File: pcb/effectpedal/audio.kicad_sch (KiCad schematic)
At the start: 5 parts

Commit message: Made progress on the PCB
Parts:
- removed J?: SJ2-3574A-SMT-TR, SJ23574ASMTTR, symbol SJ2-3574A-SMT-TR:SJ2-3574A-SMT-TR
- added C1, C2, C3, C4, C5, C6: 47u, Capacitor_SMD:C_1210_3225Metric, symbol Device:C_Small
- added C10, C11, C7, C8, C9: 0.1u, Capacitor_SMD:C_0805_2012Metric, symbol Device:C_Small
- added C12, C13: 33p, Capacitor_SMD:C_0805_2012Metric, symbol Device:C_Small
- added D1, D2, D3, D4: D_Schottky, Diode_SMD:D_0805_2012Metric, symbol Device:D_Schottky
- added J1, J2, J3: SJ-43515RS-SMT-TR, footprints:SJ43515RSSMTTR, symbol SJ-43515RS-SMT-TR:SJ-43515RS-SMT-TR
- added J10: Conn_01x06_Male, Connector_PinHeader_2.54mm:PinHeader_1x06_P2.54mm_Vertical, symbol Connector:Conn_01x06_Male
- added J11, J7, J8: Conn_01x04_Female, Connector_PinSocket_2.54mm:PinSocket_1x04_P2.54mm_Vertical, symbol Connector:Conn_01x04_Female
- added J4, J5, J6, J9: Conn_01x06_Female, Connector_PinSocket_2.54mm:PinSocket_1x06_P2.54mm_Vertical, symbol Connector:Conn_01x06_Female
- added JP1, JP10, JP11, JP12, JP13, JP14, JP16, JP17, JP18, JP19, JP20, JP22, JP23, JP24, JP25, JP26, JP29, JP30, JP31, JP4, JP49, JP5, JP50, JP6, JP7, JP8: SolderJumper_2_Open, Jumper:SolderJumper-2_P1.3mm_Open_Pad1.0x1.5mm, symbol Jumper:SolderJumper_2_Open
- added JP15, JP21, JP27, JP28, JP3, JP32, JP9: SolderJumper_2_Bridged, Jumper:SolderJumper-2_P1.3mm_Bridged2Bar_Pad1.0x1.5mm, symbol Jumper:SolderJumper_2_Bridged
- added R1, R2: 10k, Resistor_SMD:R_0805_2012Metric, symbol Device:R
- added R10, R11, R8, R9: 4k, Resistor_SMD:R_0805_2012Metric, symbol Device:R
- added R3, R5, R6, R7: 27, Resistor_SMD:R_0805_2012Metric, symbol Device:R_Small
- added R4: 10, Resistor_SMD:R_0805_2012Metric, symbol Device:R_Small
- added TP10, TP6, TP7, TP9: TestPoint, TestPoint:TestPoint_Pad_D1.0mm, symbol Connector:TestPoint
- IC1: renamed from IC?; footprint SOIC127P600X175-8N -> footprints:SOIC127P600X175-8N
- U1: renamed from U?; footprint QFN50P500X500X100-33N -> footprints:QFN50P500X500X100-33N
- U2, U3: renamed from U?; value SC0915 -> Pi Pico; footprint MODULE_SC0915 -> footprints:MODULE_SC0915
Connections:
- net MCU_DBG_TX: now reaches U2.1 (GP0)
- net MCU_DBG_TX: now also U3.7 (GP5), J10.3 (Pin_3)
- net MN_UI-INT: now reaches U2.10 (GP7)
- net MN_UI-INT: now also J9.6 (Pin_6)
- net MN_EX3: now reaches U2.11 (GP8)
- net MN_EX3: now also U3.11 (GP8), J5.2 (Pin_2), JP50.2 (B)
- net at U2.12 (GP9): now also IC1.1 (CE#)
- net GND3: now reaches U2.13 (GND), U2.18 (GND), U2.23 (GND), U2.28 (GND), U2.3 (GND), U2.38 (GND), U2.8 (GND), U2.D2 (GND)
- net GND3: now also IC1.4 (VSS), U1.12 (SPI_SELECT), U1.28 (DVSS), U1.33 (EP), U1.7 (IOVSS), U3.13 (GND), U3.18 (GND), U3.23 (GND), U3.28 (GND), U3.3 (GND), U3.38 (GND), U3.8 (GND), U3.D2 (GND), C10.1, C11.1, C9.1, J10.1 (Pin_1), J11.1 (Pin_1), J11.2 (Pin_2), J5.1 (Pin_1), J6.1 (Pin_1), J6.2 (Pin_2), J6.3 (Pin_3), J7.1 (Pin_1), J7.2 (Pin_2), J7.3 (Pin_3), J8.1 (Pin_1), J9.1 (Pin_1), JP30.1 (A), JP31.1 (A)
- net at U2.14 (GP10): now also IC1.6 (CLK)
- net at U2.15 (GP11): now also IC1.5 (SI/SIO0)
- net MN_EX4: now reaches U2.16 (GP12)
- net MN_EX4: now also U3.12 (GP9), J5.5 (Pin_5), JP49.2 (B)
- net at U2.17 (GP13): now also IC1.7 (SIO3)
- net MN_EX1: now reaches U2.19 (GP14)
- net MN_EX1: now also U3.9 (GP6), J5.3 (Pin_3)
- net MCU_DBG_RX: now reaches U2.2 (GP1)
- net MCU_DBG_RX: now also U3.6 (GP4), J10.4 (Pin_4)
- net MN_EX2: now reaches U2.20 (GP15)
- net MN_EX2: now also U3.10 (GP7), J5.4 (Pin_4)
- net at U2.21 (GP16): now also JP3.1 (A), JP4.1 (A), JP5.1 (A), JP6.1 (A), JP7.1 (A)
- net at U2.22 (GP17): now also JP10.1 (A), JP11.1 (A), JP12.1 (A), JP8.1 (A), JP9.1 (A)
- net at U2.24 (GP18): now also JP13.1 (A), JP14.1 (A), JP15.1 (A), JP16.1 (A), JP17.1 (A)
- net at U2.25 (GP19): now also JP18.1 (A), JP19.1 (A), JP20.1 (A), JP21.1 (A), JP22.1 (A)
- net at U2.26 (GP20): now also JP23.1 (A), JP24.1 (A), JP25.1 (A), JP26.1 (A), JP27.1 (A)
- net AUDIO_INT1: now reaches U2.27 (GP21)
- net AUDIO_INT1: now also U1.11 (MISO/MFP4)
- net AUDIO_INT2: now reaches U2.29 (GP22)
- net AUDIO_INT2: now also U1.32 (GPIO/MFP5_(32))
- net ADC0: now reaches U2.31 (GP26)
- net ADC0: now also J4.1 (Pin_1)
- net ADC1: now reaches U2.32 (GP27)
- net ADC1: now also J4.3 (Pin_3)
- net MN_AGND: now reaches U2.33 (AGND)
- net MN_AGND: now also J4.2 (Pin_2), J4.4 (Pin_4), JP30.2 (B)
- net ADC2: now reaches U2.34 (GP28)
- net ADC2: now also J4.5 (Pin_5)
- net MN_3V3: now reaches U2.36 (3V3_OUT)
- net MN_3V3: now also IC1.8 (VDD), U1.26 (LDOIN), U1.30 (LDO_SELECT), U1.6 (IOVDD), C11.2, C9.2, J10.2 (Pin_2), J11.3 (Pin_3), J11.4 (Pin_4), J4.6 (Pin_6), J5.6 (Pin_6), J6.4 (Pin_4), J6.5 (Pin_5), J6.6 (Pin_6), J8.2 (Pin_2), J9.2 (Pin_2), JP29.1 (A), JP32.2 (B), R10.1, R11.1, R8.1, R9.1
- net MN_UI-SDA: now reaches U2.4 (GP2)
- net MN_UI-SDA: now also J8.3 (Pin_3), J9.3 (Pin_3), R8.2
- net MN_UI-SCL: now reaches U2.5 (GP3)
- net MN_UI-SCL: now also J8.4 (Pin_4), J9.4 (Pin_4), R9.2
- net AUDIO-SDA: now reaches U2.6 (GP4)
- net AUDIO-SDA: now also U1.10 (SDA/MOSI), R10.2
- net AUDIO-SCL: now reaches U2.7 (GP5)
- net AUDIO-SCL: now also U1.9 (SCL/SSZ), R11.2
- net MN_RST: now reaches U2.9 (GP6)
- net MN_RST: now also J7.4 (Pin_4), J9.5 (Pin_5), JP28.2 (B)
- net DBG_SWCLK: now reaches U2.D1 (SWCLK)
- net DBG_SWCLK: now also U3.4 (GP2), J10.6 (Pin_6)
- net DBG_SWDIO: now reaches U2.D3 (SWDIO)
- net DBG_SWDIO: now also U3.5 (GP3), J10.5 (Pin_5)
- net at IC1.2 (SO/SIO1): now also JP50.1 (A)
- net at IC1.3 (SIO2): now also JP49.1 (A)
- net AUDIO_MCLK: now reaches U1.1 (MCLK_(1))
- net AUDIO_MCLK: now also R4.2
- net AUDIO_IN_L: now reaches U1.13 (IN1_L)
- net AUDIO_IN_L: now also C1.1, C12.2, D1.2 (A), D2.1 (K)
- net AUDIO_IN_R: now reaches U1.14 (IN1_R)
- net AUDIO_IN_R: now also C13.2, C6.1, D3.2 (A), D4.1 (K)
- net AUDIO_AGND: now reaches U1.15 (IN2_L)
- net AUDIO_AGND: now also U1.16 (IN2_R), U1.17 (AVSS), U1.20 (IN3_L), U1.21 (IN3_R), C12.1, C13.1, C7.2, C8.1, D2.2 (A), D4.2 (A), J1.1 (SLEEVE), J1.4 (RING_2_), J2.1 (SLEEVE), J3.1 (SLEEVE), J3.4 (RING_2_), JP1.1 (A), JP31.2 (B), R1.2, R2.2
- net at U1.18 (REF): now also C7.1
- net at U1.2 (BCLK): now also R5.2
- net AUDIO_LINE_L: now reaches U1.22 (LOL)
- net AUDIO_LINE_L: now also C4.1, TP10.1
- net AUDIO_LINE_R: now reaches U1.23 (LOR)
- net AUDIO_LINE_R: now also C5.1, TP7.1
- net AUDIO_AVDD: now reaches U1.24 (AVDD)
- net AUDIO_AVDD: now also C8.2, D1.1 (K), D3.1 (K)
- net HEADPHONE_L: now reaches U1.25 (HPL)
- net HEADPHONE_L: now also C2.1, TP9.1
- net HEADPHONE_R: now reaches U1.27 (HPR)
- net HEADPHONE_R: now also C3.1, TP6.1
- net at U1.29 (DVDD): now also C10.2
- net at U1.3 (WCLK): now also R7.2
- net at U1.31 (~RESET): now also JP28.1 (A), JP29.2 (B)
- net AUDIO_DIN: now reaches U1.4 (DIN/MFP1)
- net AUDIO_DIN: now also R3.1
- net at U1.5 (DOUT/MFP2): now also R6.1
- net HEADSET_DETECT: now reaches U1.8 (SCLK/MFP3)
- net HEADSET_DETECT: now also J2.4 (RING_2_), JP1.2 (B)
- net at U3.36 (3V3_OUT): now also JP32.1 (A)
- new net: C1.2, J1.2 (TIP), R1.1
- new net: C5.2, J3.3 (RING_1)
- new net: C3.2, J2.3 (RING_1)
- new net: JP11.2 (B), JP16.2 (B), JP21.2 (B), JP26.2 (B), JP6.2 (B), R3.2
- new net: C4.2, J3.2 (TIP)
- new net: C6.2, J1.3 (RING_1), R2.1
- new net: JP13.2 (B), JP18.2 (B), JP23.2 (B), JP3.2 (B), JP8.2 (B), R4.1
- new net: C2.2, J2.2 (TIP)
- new net AUDIO_BCLK: JP14.2 (B), JP19.2 (B), JP24.2 (B), JP4.2 (B), JP9.2 (B), R5.1
- new net AUDIO_DOUT: JP12.2 (B), JP17.2 (B), JP22.2 (B), JP27.2 (B), JP7.2 (B), R6.2
- new net AUDIO_WCLK: JP10.2 (B), JP15.2 (B), JP20.2 (B), JP25.2 (B), JP5.2 (B), R7.1
- no-connect marks 0 -> 50
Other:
- note added: "AC Coupling"
- note added: "Analogue inter-board bus"
- note added: "Audio CODEC"
- note added: "Audio IN"
- note added: "CRÖNCH"
- note added: "Debug port"
- note added: "Headset"
- note added: "I2C pull-ups"
- note added: "LED LHS connector"
- note added: "LED RHS connector"
- note added: "Line OUT"
- note added: "Lower-right inter-board connector"
- note added: "MCU"
- note added: "Main inter-board bus"
- note added: "Onboard debugger"
- note added: "PIO->CODEC interface matrix"
- note added: "Pull-down"
- note added: "RAM"
- note added: "RF filter"
- note added: "Structural support connector"
- note added: "Upper-left inter-board connector"
- note added: "V. protection"
- note added: "by Anton Liakhovitch"
- company: (none) -> Anton Liakhovitch
- title: (none) -> CRONCH Main Board
- moved on the sheet: IC1, U1, U2, U3

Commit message: Mostly finished PCB
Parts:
- C1, C2, C3, C4, C5, C6: Digikey Part Number (none) -> 490-16309-2-ND; Digikey Price/Stock (none) -> https://www.digikey.com/en/products/detail/murata-electroni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; MANUFACTURER (none) -> Murata Electronics; MPN (none) -> GRM32EC81C476KE15K; Manufacturer_Name (none) -> Murata Electronics; Manufacturer_Part_Number (none) -> GRM32EC81C476KE15K
- C10, C11, C7, C8, C9: Digikey Part Number (none) -> 478-1395-2-ND; Digikey Price/Stock (none) -> https://www.digikey.com/en/products/detail/kyocera-avx/0805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; MANUFACTURER (none) -> KYOCERA AVX; MPN (none) -> 08055C104KAT2A; Manufacturer_Name (none) -> KYOCERA AVX; Manufacturer_Part_Number (none) -> 08055C104KAT2A
- C12, C13: Digikey Part Number (none) -> 478-1310-2-ND; Digikey Price/Stock (none) -> 478-1310-2-ND; MANUFACTURER (none) -> KYOCERA AVX; MPN (none) -> 08055A330JAT2A; Manufacturer_Name (none) -> KYOCERA AVX; Manufacturer_Part_Number (none) -> 08055A330JAT2A
- D1, D2, D3, D4: Digikey Part Number (none) -> 478-7800-2-ND; Digikey Price/Stock (none) -> https://www.digikey.com/en/products/detail/kyocera-avx/SD08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; MANUFACTURER (none) -> KYOCERA AVX; MPN (none) -> SD0805S020S1R0; Manufacturer_Name (none) -> KYOCERA AVX; Manufacturer_Part_Number (none) -> SD0805S020S1R0
- IC1: Digikey Part Number (none) -> 706-IS66WVS2M8ALL-104NLI-ND; Digikey Price/Stock (none) -> https://www.digikey.com/en/products/detail/issi-integrated-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; MANUFACTURER (none) -> Integrated Silicon Solution Inc.; MPN (none) -> IS66WVS2M8ALL-104NLI
- J1, J2, J3: Digikey Part Number (none) -> CP-43515RSSJTR-ND; Digikey Price/Stock (none) -> https://www.digikey.com/en/products/detail/cui-devices/SJ-4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; MANUFACTURER (none) -> CUI Devices; MPN (none) -> SJ-43515RS-SMT-TR
- R1, R2: Digikey Part Number (none) -> 311-10KARTR-ND; Digikey Price/Stock (none) -> https://www.digikey.com/en/products/detail/yageo/RC0805JR-0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; MANUFACTURER (none) -> YAGEO; MPN (none) -> RC0805JR-0710KL; Manufacturer_Name (none) -> YAGEO; Manufacturer_Part_Number (none) -> RC0805JR-0710KL
- R10, R11, R8, R9: Digikey Part Number (none) -> 311-4.3KARTR-ND; Digikey Price/Stock (none) -> https://www.digikey.com/en/products/detail/yageo/RC0805JR-0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; MANUFACTURER (none) -> YAGEO; MPN (none) -> RC0805JR-074K3L; Manufacturer_Name (none) -> YAGEO; Manufacturer_Part_Number (none) -> RC0805JR-074K3L
- R3, R5, R6, R7: Digikey Part Number (none) -> 311-27.0CRTR-ND; Digikey Price/Stock (none) -> https://www.digikey.com/en/products/detail/yageo/RC0805FR-0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; MANUFACTURER (none) -> YAGEO; MPN (none) -> RC0805FR-0727RL; Manufacturer_Name (none) -> YAGEO; Manufacturer_Part_Number (none) -> RC0805FR-0727RL
- R4: Digikey Part Number (none) -> 13-RC0805FR-1010RLTR-ND; Digikey Price/Stock (none) -> https://www.digikey.com/en/products/detail/yageo/RC0805FR-1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; MANUFACTURER (none) -> YAGEO; MPN (none) -> RC0805FR-1010RL; Manufacturer_Name (none) -> YAGEO; Manufacturer_Part_Number (none) -> RC0805FR-1010RL
- U1: Digikey Part Number (none) -> 296-23776-2-ND; Digikey Price/Stock (none) -> https://www.digikey.com/en/products/detail/texas-instrument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; MANUFACTURER (none) -> Texas Instruments; Manufacturer_Name (none) -> Texas Instruments; Manufacturer_Part_Number (none) -> TLV320AIC3254IRHBT; SUPPLIER Texas Instruments -> (none)
- U2, U3: Digikey Part Number (none) -> 2648-SC0915TR-ND; Digikey Price/Stock (none) -> https://www.digikey.com/en/products/detail/raspberry-pi/SC0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; MANUFACTURER Pi Supply -> Raspberry Pi; MPN (none) -> SC0915; Manufacturer_Name (none) -> Raspberry Pi; Manufacturer_Part_Number (none) -> SC0915; STANDARD Manufacturer Recommendations -> (none)

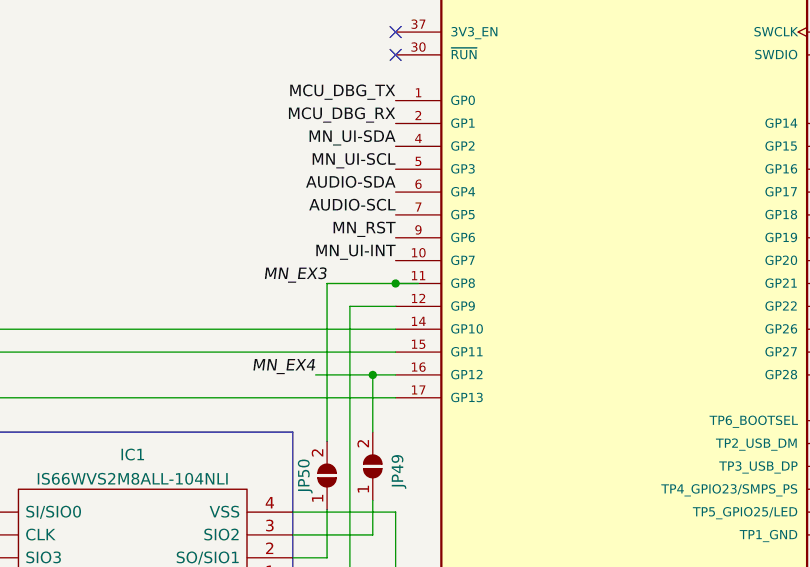
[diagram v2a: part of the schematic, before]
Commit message: Added more test code and deleted some useless stuff
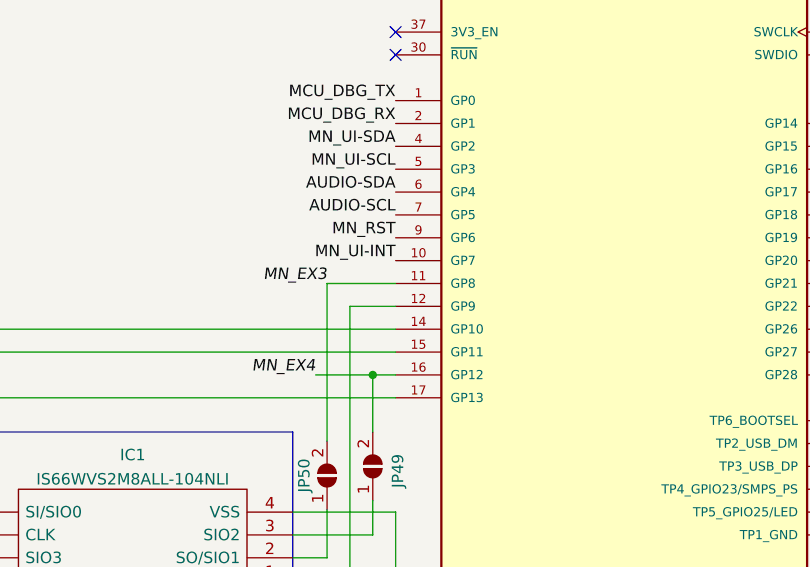
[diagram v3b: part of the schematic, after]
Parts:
- C12, C13: Digikey Price/Stock 478-1310-2-ND -> https://www.digikey.com/en/products/detail/kyocera-avx/0805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
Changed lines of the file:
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@@
   (junction (at 368.3 151.13) (diameter 0) (color 0 0 0 0)
   )
-  (junction (at 267.97 147.32) (diameter 0) (color 0 0 0 0)
-  )
   (junction (at 355.6 151.13) (diameter 0) (color 0 0 0 0)
   )
@@
     (stroke (width 0) (type default) (color 0 0 0 0))
   )
-  (wire (pts (xy 270.51 147.32) (xy 267.97 147.32))
-    (stroke (width 0) (type default) (color 0 0 0 0))
-  )
   (wire (pts (xy 35.56 125.73) (xy 45.72 125.73))
     (stroke (width 0) (type default) (color 0 0 0 0))
@@
       (effects (font (size 1.27 1.27)) hide)
     )
+    (property "Description" "Tolerance 10%, low A/V" (id 10) (at 45.72 40.64 0)
+      (effects (font (size 1.27 1.27)) hide)
+    )
     (pin "1")
     (pin "2")
@@
       (effects (font (size 1.27 1.27)) hide)
     )
+    (property "Description" "Tolerance 10%, low A/V" (id 10) (at 102.87 118.11 0)
+      (effects (font (size 1.27 1.27)) hide)
+    )
     (pin "1")
     (pin "2")
@@
       (effects (font (size 1.27 1.27)) hide)
     )
+    (property "Description" "Tolerance 10%, low A/V" (id 10) (at 167.64 52.07 0)
+      (effects (font (size 1.27 1.27)) hide)
+    )
     (pin "1")
     (pin "2")
@@
       (effects (font (size 1.27 1.27)) hide)
     )
+    (property "Description" "Forward voltage < 500mV" (id 10) (at 36.83 64.77 0)
+      (effects (font (size 1.27 1.27)) hide)
+    )
     (pin "1")
     (pin "2")
@@
       (effects (font (size 1.27 1.27)) hide)
     )
+    (property "Description" "Forward voltage < 500mV" (id 10) (at 36.83 45.72 0)
+      (effects (font (size 1.27 1.27)) hide)
+    )
     (pin "1")
     (pin "2")
@@
       (effects (font (size 1.27 1.27)) hide)
     )
-    (property "Digikey Price/Stock" "478-1310-2-ND" (id 5) (at 113.03 156.21 0)
+    (property "Digikey Price/Stock" "https://www.digikey.com/en/products/detail/kyocera-avx/08055A330JAT2A/563420?s=N4IgTCBcDaICwHYAcBaAjAZjQBhWFAcgCIgC6AvkA" (id 5) (at 113.03 156.21 0)
       (effects (font (size 1.27 1.27)) hide)
     )
@@
       (effects (font (size 1.27 1.27)) hide)
     )
+    (property "Description" "Tolerance 10%, low A/V" (id 10) (at 113.03 156.21 0)
+      (effects (font (size 1.27 1.27)) hide)
+    )
     (pin "1")
     (pin "2")
@@
       (effects (font (size 1.27 1.27)) hide)
     )
+    (property "Description" "Tolerance 10%, low A/V" (id 10) (at 114.3 52.07 0)
+      (effects (font (size 1.27 1.27)) hide)
+    )
     (pin "1")
     (pin "2")
@@
       (effects (font (size 1.27 1.27)) hide)
     )
+    (property "Description" "Tolerance 10%, low A/V" (id 10) (at 367.03 213.36 0)
+      (effects (font (size 1.27 1.27)) hide)
+    )
     (pin "1")
     (pin "2")
@@
       (effects (font (size 1.27 1.27)) hide)
     )
+    (property "Description" "Tolerance 2%, low A/V" (id 10) (at 121.92 120.65 0)
+      (effects (font (size 1.27 1.27)) hide)
+    )
     (pin "1")
     (pin "2")
@@
       (effects (font (size 1.27 1.27)) hide)
     )
+    (property "Description" "Tolerance 2%, low A/V" (id 10) (at 198.12 123.19 0)
+      (effects (font (size 1.27 1.27)) hide)
+    )
     (pin "1")
     (pin "2")
@@
       (effects (font (size 1.27 1.27)) hide)
     )
+    (property "Description" "Tolerance 10%, low A/V" (id 10) (at 52.07 73.66 0)
+      (effects (font (size 1.27 1.27)) hide)
+    )
     (pin "1")
     (pin "2")
@@
       (effects (font (size 1.27 1.27)) hide)
     )
+    (property "Description" "Tolerance 10%, low A/V" (id 10) (at 367.03 218.44 0)
+      (effects (font (size 1.27 1.27)) hide)
+    )
     (pin "1")
     (pin "2")
@@
       (effects (font (size 1.27 1.27)) hide)
     )
+    (property "Description" "Tolerance 10%, low A/V" (id 10) (at 93.98 118.11 0)
+      (effects (font (size 1.27 1.27)) hide)
+    )
     (pin "1")
     (pin "2")
@@
       (effects (font (size 1.27 1.27)) hide)
     )
+    (property "Description" "Tolerance 10%, low A/V" (id 10) (at 45.72 69.85 0)
+      (effects (font (size 1.27 1.27)) hide)
+    )
     (pin "1")
     (pin "2")
@@
       (effects (font (size 1.27 1.27)) hide)
     )
+    (property "Description" "Tolerance 10%, low A/V" (id 10) (at 200.66 105.41 0)
+      (effects (font (size 1.27 1.27)) hide)
+    )
     (pin "1")
     (pin "2")
@@
       (effects (font (size 1.27 1.27)) hide)
     )
+    (property "Description" "Tolerance 10%, low A/V" (id 10) (at 367.03 223.52 0)
+      (effects (font (size 1.27 1.27)) hide)
+    )
     (pin "1")
     (pin "2")
@@
       (effects (font (size 1.27 1.27)) hide)
     )
-    (property "Digikey Price/Stock" "478-1310-2-ND" (id 5) (at 123.19 156.21 0)
+    (property "Digikey Price/Stock" "https://www.digikey.com/en/products/detail/kyocera-avx/08055A330JAT2A/563420?s=N4IgTCBcDaICwHYAcBaAjAZjQBhWFAcgCIgC6AvkA" (id 5) (at 123.19 156.21 0)
       (effects (font (size 1.27 1.27)) hide)
     )
@@
       (effects (font (size 1.27 1.27)) hide)
     )
+    (property "Description" "Tolerance 10%, low A/V" (id 10) (at 123.19 156.21 0)
+      (effects (font (size 1.27 1.27)) hide)
+    )
     (pin "1")
     (pin "2")
@@
       (effects (font (size 1.27 1.27)) hide)
     )
+    (property "Description" "Tolerance 10%, low A/V" (id 10) (at 367.03 228.6 0)
+      (effects (font (size 1.27 1.27)) hide)
+    )
     (pin "1")
     (pin "2")
@@
       (effects (font (size 1.27 1.27)) hide)
     )
+    (property "Description" "Tolerance 2%, low A/V" (id 10) (at 353.06 109.22 0)
+      (effects (font (size 1.27 1.27)) hide)
+    )
     (pin "1")
     (pin "2")
@@
       (effects (font (size 1.27 1.27)) hide)
     )
+    (property "Description" "Tolerance 10%, low A/V" (id 10) (at 125.73 107.95 0)
+      (effects (font (size 1.27 1.27)) hide)
+    )
     (pin "1")
     (pin "2")
@@
       (effects (font (size 1.27 1.27)) hide)
     )
+    (property "Description" "Tolerance 2%, low A/V" (id 10) (at 121.92 124.46 0)
+      (effects (font (size 1.27 1.27)) hide)
+    )
     (pin "1")
     (pin "2")
@@
       (effects (font (size 1.27 1.27)) hide)
     )
+    (property "Description" "Tolerance 10%, low A/V" (id 10) (at 93.98 133.35 0)
+      (effects (font (size 1.27 1.27)) hide)
+    )
     (pin "1")
     (pin "2")
@@
       (effects (font (size 1.27 1.27)) hide)
     )
+    (property "Description" "Tolerance 10%, low A/V" (id 10) (at 160.02 52.07 0)
+      (effects (font (size 1.27 1.27)) hide)
+    )
     (pin "1")
     (pin "2")
@@
       (effects (font (size 1.27 1.27)) hide)
     )
+    (property "Description" "Forward voltage < 500mV" (id 10) (at 36.83 35.56 0)
+      (effects (font (size 1.27 1.27)) hide)
+    )
     (pin "1")
     (pin "2")
@@
       (effects (font (size 1.27 1.27)) hide)
     )
+    (property "Description" "Tolerance 10%, low A/V" (id 10) (at 52.07 44.45 0)
+      (effects (font (size 1.27 1.27)) hide)
+    )
     (pin "1")
     (pin "2")
@@
       (effects (font (size 1.27 1.27)) hide)
     )
+    (property "Description" "Tolerance 2%, low A/V" (id 10) (at 358.14 95.25 0)
+      (effects (font (size 1.27 1.27)) hide)
+    )
     (pin "1")
     (pin "2")
@@
       (effects (font (size 1.27 1.27)) hide)
     )
+    (property "Description" "Forward voltage < 500mV" (id 10) (at 36.83 74.93 0)
+      (effects (font (size 1.27 1.27)) hide)
+    )
     (pin "1")
     (pin "2")
@@
       (effects (font (size 1.27 1.27)) hide)
     )
+    (property "Description" "Tolerance 10%, low A/V" (id 10) (at 106.68 52.07 0)
+      (effects (font (size 1.27 1.27)) hide)
+    )
